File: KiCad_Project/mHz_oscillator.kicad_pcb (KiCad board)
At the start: 2 copper layers, 63.5 x 92.7 mm, 128 parts, among them J1 Conn_01x06_Male, J10 Conn_01x05_Female, J11 Conn_02x08_Odd_Even, J12 Saw, J13 Sqaure, J14 Triangle, J15 Sine, J16 Trigger, J17 CV_in, J2 Conn_01x06_Female, J3 Conn_01x06_Male, J4 Conn_01x06_Female, J5 Conn_01x06_Male, J6 Conn_01x06_Female, J7 Conn_01x05_Male, J8 Conn_01x05_Female, J9 Conn_01x05_Male, Q1 BC847, Q2 BC847, SW1 Trigger Button, SW2 Freq Range, SW3 One Shot or Continous, U1 LM324, U2 4013, U3 LM324, U4 4071, U5 LM324, U6 LM324, U7 LM311, U8 LM324

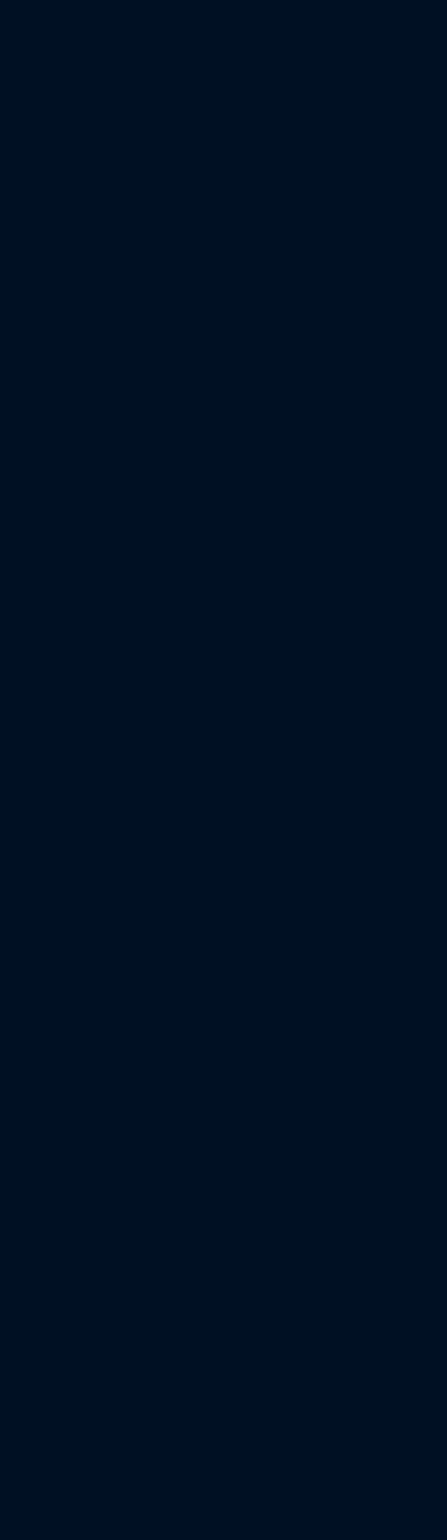
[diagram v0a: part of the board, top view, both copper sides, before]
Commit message: update pcb with frontpanel design
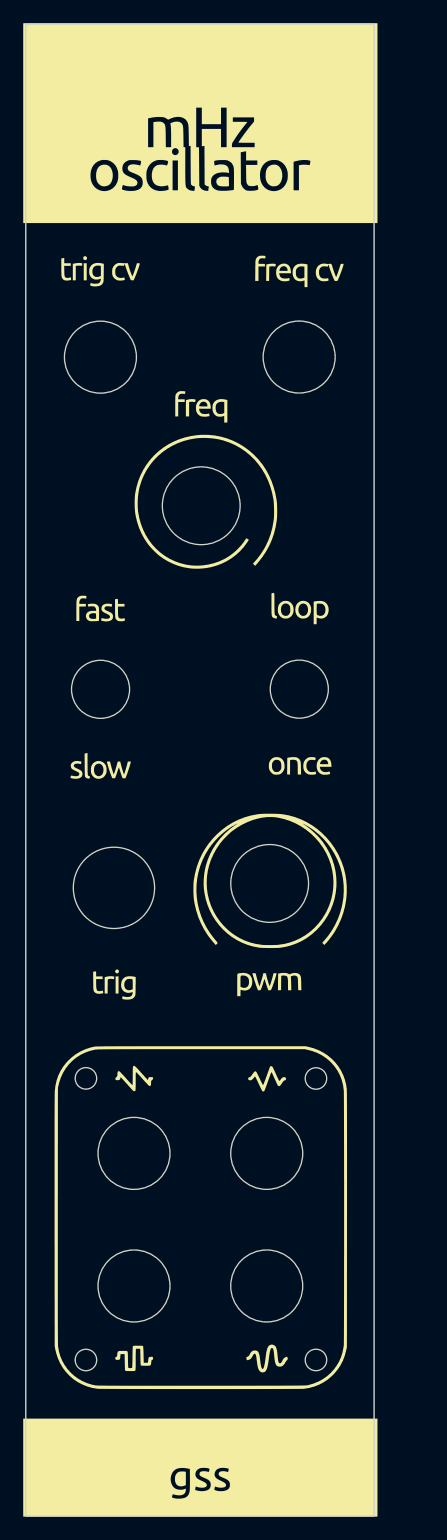
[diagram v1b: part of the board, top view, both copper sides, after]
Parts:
- added ?: , , F.Cu at (-4.14, 6.38)
- added ?: , , F.Cu at (15.7, -17.9)
- added ?: , , F.Cu at (15.7, 6.37)
- added G***: LOGO, frontpanel:frontpanel, F.Cu at (-49.5, 19.9)
- added REF**: PJ392_Drill_Hole_Panel, OS_Drill_Holes:PJ392_Drill_Hole_Panel, F.Cu at (-2.89, -80.0)
- added REF**: PJ392_Drill_Hole_Panel, OS_Drill_Holes:PJ392_Drill_Hole_Panel, F.Cu at (-40.0, 0.00)
- added REF**: PJ392_Drill_Hole_Panel, OS_Drill_Holes:PJ392_Drill_Hole_Panel, F.Cu at (0.00, -11.4)
- added REF**: SMTS_102_Drill_Hole_Panel, OS_Drill_Holes:SMTS_102_Drill_Hole_Panel, F.Cu at (14.2, -51.4)
- added REF**: PJ392_Drill_Hole_Panel, OS_Drill_Holes:PJ392_Drill_Hole_Panel, F.Cu at (-28.6, -11.4)
- added REF**: LED_1.8mm_Drill_Hole_Panel, OS_Drill_Holes:LED_1.8mm_Drill_Hole_Panel, F.Cu at (-4.14, -17.9)
- added REF**: RK097_Drill_Hole_Panel, OS_Drill_Holes:RK097_Drill_Hole_Panel, F.Cu at (5.79, -67.2)
- added REF**: 6HP_Front_Panel, OS_Front_Panels:6HP_Front_Panel, F.Cu at (-49.3, -108.7)
- added REF**: PJ392_Drill_Hole_Panel, OS_Drill_Holes:PJ392_Drill_Hole_Panel, F.Cu at (14.2, -80.0)
- added REF**: SMTS_102_Drill_Hole_Panel, OS_Drill_Holes:SMTS_102_Drill_Hole_Panel, F.Cu at (-2.88, -51.4)
- added REF**: PJ392_Drill_Hole_Panel, OS_Drill_Holes:PJ392_Drill_Hole_Panel, F.Cu at (11.4, 0.00)
- added REF**: RK097_Drill_Hole_Panel, OS_Drill_Holes:RK097_Drill_Hole_Panel, F.Cu at (11.7, -34.7)
- added REF**: PBS_110_Drill_Hole_Panel, OS_Drill_Holes:PBS_110_Drill_Hole_Panel, F.Cu at (-1.73, -34.3)

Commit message: add files
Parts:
- removed the    at (48.3, 7.02) (x2)
- removed the    at (31.8, 7.02) (x2)
- moved G*** 67.8 mm to (-27.7, -44.3)
- moved J2 20.4 mm to (53.0, 8.26), turned to -90 degrees
- moved J1 20.4 mm to (18.7, 8.26), turned to 90 degrees
- moved REF** 15.1 mm to (8.88, -10.2)
- moved R16 14.4 mm to (51.8, 4.45), turned to 180 degrees
- moved ? 13.2 mm to (8.88, 4.13)
- moved ? 11.4 mm to (24.1, -10.2)
- moved D8 10.9 mm to (1.32, -9.26), turned to 45 degrees
- moved REF** 9.03 mm to (-20.0, -14.3)
- moved D10 8.81 mm to (16.6, -9.26), turned to 45 degrees
- moved ? 8.75 mm to (24.1, 4.13)
- moved REF** 8.57 mm to (20.0, 0.00)
- moved REF** 8.48 mm to (20.0, -33.0)
- moved R32 8.13 mm to (43.2, 4.45), turned to 180 degrees
- moved REF** 7.79 mm to (4.76, -49.8)
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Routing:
- net /main_pcb/Triangle_LEDCathode: track 10.2 -> 26.0 mm
- net /interface_pcb/Triangle: track 6.52 -> 22.0 mm
- net /interface_pcb/Triangle_LEDAnode: track 5.82 -> 20.8 mm
- net /interface_pcb/Freq_CW: track 7.15 -> 17.5 mm
- net /interface_pcb/Triangle_LEDCathode: track 9.41 -> 19.0 mm
- net /main_pcb/Sine: track 32.9 -> 25.5 mm
- net /interface_pcb/Sine: track 3.48 -> 10.2 mm
- net /interface_pcb/Sine_LEDAnode: track 12.5 -> 6.79 mm
- net /interface_pcb/Freq_CCW: track 15.1 -> 9.95 mm
- net /interface_pcb/Saw_LEDAnode: track 6.98 -> 11.3 mm
- net /main_pcb/Triangle: track 13.6 -> 17.3 mm
- net /interface_pcb/Square: track 3.48 -> 6.17 mm
- net /interface_pcb/Square_LEDCathode: track 9.91 -> 12.6 mm
- net /interface_pcb/Sine_LEDCathode: track 13.7 -> 11.9 mm
- net /interface_pcb/Freq_Low: track 19.1 -> 20.8 mm
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- added copper zone on F.Cu, net (none)
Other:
- board size 63.5 x 92.7 mm -> 63.5 x 94.3 mm
